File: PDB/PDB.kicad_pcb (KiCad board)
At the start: 2 copper layers, 0 parts

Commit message: more footprint
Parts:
- added C1: 4.7uF, Capacitor_SMD:C_0603_1608Metric, F.Cu at (390.8, 77.3)
- added C10: 470nF, Capacitor_SMD:C_0603_1608Metric, F.Cu at (394.8, 84.8)
- added C11: 470nF, Capacitor_SMD:C_0603_1608Metric, F.Cu at (394.8, 87.3)
- added C12: 1.5uF, Capacitor_SMD:C_0603_1608Metric, F.Cu at (394.8, 89.8)
- added C13: 1.5uF, Capacitor_SMD:C_0603_1608Metric, F.Cu at (398.9, 77.3)
- added C14: 100nf, Capacitor_SMD:C_0603_1608Metric, F.Cu at (398.9, 79.8)
- added C15: 100nf, Capacitor_SMD:C_0603_1608Metric, F.Cu at (424.1, 104.4)
- added C16: 100nf, Capacitor_SMD:C_0603_1608Metric, F.Cu at (438.6, 132.3)
- added C17: 100nf, Capacitor_SMD:C_0603_1608Metric, F.Cu at (424.1, 132.3)
- added C18: 100nf, Capacitor_SMD:C_0603_1608Metric, F.Cu at (377.8, 104.4)
- added C19: 100nf, Capacitor_SMD:C_0603_1608Metric, F.Cu at (377.8, 106.9)
- added C2: 100nF, Capacitor_SMD:C_0603_1608Metric, F.Cu at (390.8, 79.8)
- added C20: 4.7uF, Capacitor_SMD:C_0603_1608Metric_Pad1.08x0.95mm_HandSolder, F.Cu at (320.8, 104.4)
- added C21: 470nF, Capacitor_SMD:C_0603_1608Metric_Pad1.08x0.95mm_HandSolder, F.Cu at (320.8, 106.9)
- added C22: 2.2uF, Capacitor_SMD:C_0603_1608Metric_Pad1.08x0.95mm_HandSolder, F.Cu at (320.8, 109.4)
- added C23: 470nF, Capacitor_SMD:C_0603_1608Metric_Pad1.08x0.95mm_HandSolder, F.Cu at (320.8, 111.9)
- added C24: 68uF, Capacitor_SMD:C_0603_1608Metric_Pad1.08x0.95mm_HandSolder, F.Cu at (320.8, 114.4)
- added C25: 68uF, Capacitor_SMD:C_0603_1608Metric_Pad1.08x0.95mm_HandSolder, F.Cu at (320.8, 116.9)
- added C26: 68uF, Capacitor_SMD:C_0603_1608Metric_Pad1.08x0.95mm_HandSolder, F.Cu at (320.8, 119.4)
- added C27: 470nF, Capacitor_SMD:C_0603_1608Metric_Pad1.08x0.95mm_HandSolder, F.Cu at (320.8, 122.0)
- added C28: 10uF, Capacitor_SMD:C_0603_1608Metric_Pad1.08x0.95mm_HandSolder, F.Cu at (320.8, 124.5)
- added C29: 10uF, Capacitor_SMD:C_0603_1608Metric_Pad1.08x0.95mm_HandSolder, F.Cu at (325.2, 104.4)
- added C3: 100nF, Capacitor_SMD:C_0603_1608Metric, F.Cu at (390.8, 82.3)
- added C30: 220nF, Capacitor_SMD:C_0603_1608Metric_Pad1.08x0.95mm_HandSolder, F.Cu at (325.2, 106.9)
- added C31: 100nF, Capacitor_SMD:C_0603_1608Metric_Pad1.08x0.95mm_HandSolder, F.Cu at (325.2, 109.4)
- added C32: 100pF, Capacitor_SMD:C_0603_1608Metric_Pad1.08x0.95mm_HandSolder, F.Cu at (325.2, 111.9)
- added C33: 220uF, Capacitor_SMD:C_0603_1608Metric_Pad1.08x0.95mm_HandSolder, F.Cu at (325.2, 114.4)
- added C34: 10uF, Capacitor_SMD:C_0603_1608Metric_Pad1.08x0.95mm_HandSolder, F.Cu at (325.2, 116.9)
- added C35: 1uF, Capacitor_SMD:C_0603_1608Metric_Pad1.08x0.95mm_HandSolder, F.Cu at (325.2, 119.4)
- added C36: 1uF, Capacitor_SMD:C_0603_1608Metric_Pad1.08x0.95mm_HandSolder, F.Cu at (325.2, 122.0)
- added C37: 1uF, Capacitor_SMD:C_0603_1608Metric_Pad1.08x0.95mm_HandSolder, F.Cu at (325.2, 124.5)
- added C38: 100nf, Capacitor_SMD:C_0603_1608Metric, F.Cu at (332.8, 127.0)
- added C39: 10uF, Capacitor_SMD:C_0603_1608Metric_Pad1.08x0.95mm_HandSolder, F.Cu at (329.5, 104.4)
- added C4: 100nF, Capacitor_SMD:C_0603_1608Metric, F.Cu at (390.8, 84.8)
- added C40: 100nf, Capacitor_SMD:C_0603_1608Metric, F.Cu at (391.9, 104.4)
- added C5: 100nF, Capacitor_SMD:C_0603_1608Metric, F.Cu at (390.8, 87.3)
- added C6: 100nF, Capacitor_SMD:C_0603_1608Metric, F.Cu at (390.8, 89.8)
- added C7: 100nF, Capacitor_SMD:C_0603_1608Metric, F.Cu at (394.8, 77.3)
- added C8: 2.2uF, Capacitor_SMD:C_0603_1608Metric, F.Cu at (394.8, 79.8)
- added C9: 2.2uF, Capacitor_SMD:C_0603_1608Metric, F.Cu at (394.8, 82.3)
- added Cboot1: 08053C104KAT2A, Capacitor_SMD:C_0603_1608Metric, F.Cu at (424.1, 106.9)
- added Cboot2: 470nF, Capacitor_SMD:C_0603_1608Metric, F.Cu at (438.6, 134.8)
- added Cboot3: 100nF, Capacitor_SMD:C_0603_1608Metric, F.Cu at (377.8, 109.4)
- added Cboot4: 08053C104JAZ2A, Capacitor_SMD:C_0603_1608Metric, F.Cu at (391.9, 106.9)
- added Ccomp1: C0402C150J4GACTU, Capacitor_SMD:C_0603_1608Metric, F.Cu at (424.1, 109.4)
- added Ccomp2: 04025A471JAT2A, Capacitor_SMD:C_0603_1608Metric, F.Cu at (424.1, 111.9)
- added Ccomp3: 47nF, Capacitor_SMD:C_0603_1608Metric, F.Cu at (377.8, 111.9)
- added Ccomp4: 820pF, Capacitor_SMD:C_0603_1608Metric, F.Cu at (377.8, 114.4)
- added Ccomp5: CGA4J2C0G1H333J125AA, Capacitor_SMD:C_0603_1608Metric, F.Cu at (391.9, 109.4)
- added Ccomp6: GRM1555C1H391JA01J, Capacitor_SMD:C_0603_1608Metric, F.Cu at (391.9, 111.9)
- added Cin1: C3225X7R2A225K230AB, Capacitor_SMD:C_0603_1608Metric, F.Cu at (424.1, 114.4)
- added Cin2: 4.7uF, Capacitor_SMD:C_0603_1608Metric, F.Cu at (438.6, 137.3)
- added Cin3: 4.7 uF, Capacitor_SMD:C_0603_1608Metric, F.Cu at (424.1, 134.8)
- added Cin4: 15uF, Capacitor_SMD:C_0603_1608Metric, F.Cu at (377.8, 116.9)
- added Cin5: 100SXV15M, Capacitor_SMD:C_0603_1608Metric, F.Cu at (391.9, 114.4)
- added Cin_1: 100SXV15M, Capacitor_SMD:C_0603_1608Metric, F.Cu at (391.9, 116.9)
- added Cin_2: 100SXV15M, Capacitor_SMD:C_0603_1608Metric, F.Cu at (391.9, 119.4)
- added Cinx1: C2012X7R2A104K125AA, Capacitor_SMD:C_0603_1608Metric, F.Cu at (428.1, 104.4)
- added Cinx2: 470nF, Capacitor_SMD:C_0603_1608Metric, F.Cu at (438.6, 139.8)
- added Cinx3: 100nF, Capacitor_SMD:C_0603_1608Metric, F.Cu at (377.8, 119.4)
- added Cinx4: C2012X7R2A104K125AA, Capacitor_SMD:C_0603_1608Metric, F.Cu at (395.9, 104.4)
- added Cout1: GRM32ER61C476KE15L, Capacitor_SMD:C_0603_1608Metric, F.Cu at (428.1, 106.9)
- added Cout2: 220uF, Capacitor_SMD:C_0603_1608Metric, F.Cu at (442.6, 132.3)
- added Cout3: 22uF, Capacitor_SMD:C_0603_1608Metric, F.Cu at (424.1, 137.3)
- added Cout4: 22uF, Capacitor_SMD:C_0603_1608Metric, F.Cu at (377.8, 122.0)
- added Cout5: EEHZC1E331P, Capacitor_SMD:C_0603_1608Metric, F.Cu at (395.9, 106.9)
- added Cout_1: GRM32ER61C476KE15L, Capacitor_SMD:C_0603_1608Metric, F.Cu at (428.1, 109.4)
- added Cout_2: EEHZC1E331P, Capacitor_SMD:C_0603_1608Metric, F.Cu at (395.9, 109.4)
- added Coutx1: 470nF, Capacitor_SMD:C_0603_1608Metric, F.Cu at (442.6, 134.8)
- added Coutx2: 470nF, Capacitor_SMD:C_0603_1608Metric, F.Cu at (381.8, 104.4)
- added Coutx3: 470nF, Capacitor_SMD:C_0603_1608Metric, F.Cu at (381.8, 106.9)
- added Coutx4: C1005X6S1C474K050BC, Capacitor_SMD:C_0603_1608Metric, F.Cu at (395.9, 111.9)
- added Coutx5: C1005X6S1C474K050BC, Capacitor_SMD:C_0603_1608Metric, F.Cu at (395.9, 114.4)
- added Cramp1: GRM1555C1H241GA01D, Capacitor_SMD:C_0603_1608Metric, F.Cu at (428.1, 111.9)
- added Cramp2: 680pF, Capacitor_SMD:C_0603_1608Metric, F.Cu at (381.8, 109.4)
- added Cramp3: CL05C821JB5NNNC, Capacitor_SMD:C_0603_1608Metric, F.Cu at (395.9, 116.9)
- added Css1: CGA4J2C0G1H333J125AA, Capacitor_SMD:C_0603_1608Metric, F.Cu at (428.1, 114.4)
- added Css2: 22nF, Capacitor_SMD:C_0603_1608Metric, F.Cu at (381.8, 111.9)
- added Css3: C2012C0G1H223K125AA, Capacitor_SMD:C_0603_1608Metric, F.Cu at (395.9, 119.4)
- added Cvcc1: C1005X5R1E105K050BC, Capacitor_SMD:C_0603_1608Metric, F.Cu at (432.1, 104.4)
- added Cvcc2: 2.2uF, Capacitor_SMD:C_0603_1608Metric, F.Cu at (442.6, 137.3)
- added Cvcc3: 1uF, Capacitor_SMD:C_0603_1608Metric, F.Cu at (381.8, 114.4)
- added Cvcc4: C1005X5R1E105K050BC, Capacitor_SMD:C_0603_1608Metric, F.Cu at (399.9, 104.4)
- added D1: LED, LED_SMD:LED_0805_2012Metric, F.Cu at (407.1, 77.5)
- added D10: DDZ9699T 12V, Diode_SMD:D_SOD-523, F.Cu at (451.6, 77.3)
- added D11: DDZ9699T 12V, Diode_SMD:D_SOD-523, F.Cu at (451.6, 79.7)
- added D12: BAS516,115, Diode_SMD:D_SOD-523, F.Cu at (441.5, 121.0)
- added D13: LED, LED_SMD:LED_0805_2012Metric, F.Cu at (440.4, 125.5)
- added D14: LED, LED_SMD:LED_0805_2012Metric, F.Cu at (450.9, 132.6)
- added D15: LED, LED_SMD:LED_0805_2012Metric, F.Cu at (428.4, 143.9)
- added D16: 850mV, Diode_SMD:D_SOD-523, F.Cu at (385.0, 124.4)
- added D17: 950mV, Diode_SMD:D_SOD-523, F.Cu at (385.0, 126.9)
- added D18: LED, LED_SMD:LED_0805_2012Metric, F.Cu at (368.9, 128.3)
- added D19: STPS5L25B, Package_TO_SOT_SMD:TO-252-2, F.Cu at (325.6, 129.9)
- added D2: LED, LED_SMD:LED_0805_2012Metric, F.Cu at (407.1, 80.6)
- added D20: LED, LED_SMD:LED_0805_2012Metric, F.Cu at (350.4, 129.6)
- added D21: SBRD10200TR, Package_TO_SOT_SMD:TO-252-2_TabPin1, F.Cu at (413.8, 107.6)
- added D22: SB20150TR, Diode_THT:D_5W_P10.16mm_Horizontal, F.Cu at (392.0, 123.3)
- added D23: LED, LED_SMD:LED_0805_2012Metric, F.Cu at (416.6, 129.8)
- added D3: LED, LED_SMD:LED_0805_2012Metric, F.Cu at (407.1, 83.6)
- added D4: LED, LED_SMD:LED_0805_2012Metric, F.Cu at (407.1, 86.7)
- added D5: LED, LED_SMD:LED_0805_2012Metric, F.Cu at (407.1, 89.7)
- added D6: SMAJ64A, Diode_SMD:D_SMA, F.Cu at (362.4, 78.3)
- added D7: SMAJ64A, Diode_SMD:D_SMA, F.Cu at (362.4, 82.9)
- added D8: SMAJ64A, Diode_SMD:D_SMA, F.Cu at (362.4, 87.4)
- added D9: SMAJ64A, Diode_SMD:D_SMA, F.Cu at (362.4, 92.0)
- added F1: TR/3216FF15-R, Fuse:Fuse_1206_3216Metric, F.Cu at (441.0, 111.5)
- added F2: TR/3216FF15-R, Fuse:Fuse_1206_3216Metric, F.Cu at (446.7, 146.2)
- added F3: TR/3216FF15-R, Fuse:Fuse_1206_3216Metric, F.Cu at (428.9, 140.7)
- added F4: TR/3216FF15-R, Fuse:Fuse_1206_3216Metric, F.Cu at (363.8, 128.4)
- added F5: TR/3216FF15-R, Fuse:Fuse_1206_3216Metric, F.Cu at (345.2, 130.7)
- added F6: TR/3216FF15-R, Fuse:Fuse_1206_3216Metric, F.Cu at (417.1, 126.6)
- added J1: Micro_SD_Card, Connector_Card:microSD_HC_Hirose_DM3AT-SF-PEJM5, F.Cu at (331.4, 85.4)
- added J13: RJ45_Abracon_ARJP11A-MASA-B-A-EMU2, Connector_RJ:RJ45_Abracon_ARJP11A-MA_Horizontal, F.Cu at (359.8, 106.0)
- added J14: USB_C_Receptacle, Connector_USB:USB_C_Receptacle_CNCTech_C-ARA1-AK51X, F.Cu at (341.9, 108.5)
- added J15: XT90PW-M, Connector_AMASS:AMASS_XT90PW-M_1x02_P10.90mm_Horizontal, F.Cu at (324.6, 71.4)
- added J16: XT90PW-M, Connector_AMASS:AMASS_XT90PW-M_1x02_P10.90mm_Horizontal, F.Cu at (347.5, 71.4)
- added J17: XT90PW-M, Connector_AMASS:AMASS_XT90PW-M_1x02_P10.90mm_Horizontal, F.Cu at (370.3, 71.4)
- added J18: XT90PW-M, Connector_AMASS:AMASS_XT90PW-M_1x02_P10.90mm_Horizontal, F.Cu at (393.2, 71.4)
- added J19: XT90PW-M, Connector_AMASS:AMASS_XT90PW-M_1x02_P10.90mm_Horizontal, F.Cu at (416.0, 71.4)
- added J2: XT30PW-M, Connector_AMASS:AMASS_XT30U-F_1x02_P5.0mm_Vertical, F.Cu at (412.9, 79.7)
- added J20: XT90PW-M, Connector_AMASS:AMASS_XT90PW-M_1x02_P10.90mm_Horizontal, F.Cu at (438.9, 71.4)
- added J3: XT30PW-M, Connector_AMASS:AMASS_XT30U-F_1x02_P5.0mm_Vertical, F.Cu at (412.9, 86.9)
- added J4: XT60PW-M, Connector_AMASS:AMASS_XT60-F_1x02_P7.20mm_Vertical, F.Cu at (376.5, 81.2)
- added J6: UART OUT, Connector_PinHeader_2.54mm:PinHeader_1x04_P2.54mm_Vertical, F.Cu at (423.9, 84.3)
- added J9: swd, Connector_PinHeader_2.54mm:PinHeader_1x02_P2.54mm_Vertical, F.Cu at (442.3, 78.3)
- added L1: XAL7070-222MEB, Inductor_SMD:L_1206_3216Metric, F.Cu at (441.0, 108.2)
- added L2: 8.2uH, Inductor_SMD:L_1206_3216Metric, F.Cu at (446.8, 142.8)
- added L3: 1uH, Inductor_SMD:L_1206_3216Metric, F.Cu at (429.0, 137.4)
- added L4: 33uH, Inductor_SMD:L_1206_3216Metric, F.Cu at (358.2, 128.5)
- added L5: 10uH, Inductor_SMD:L_1206_3216Metric, F.Cu at (345.3, 123.9)
- added L6: 10uH, Inductor_SMD:L_1206_3216Metric, F.Cu at (345.3, 127.3)
- added L7: 15uH, Inductor_SMD:L_1206_3216Metric, F.Cu at (400.0, 127.7)
- added M1: GENERIC_MOSFET_N, Package_SON:Infineon_PG-TDSON-8_6.15x5.15mm, F.Cu at (426.7, 119.0)
- added M2: GENERIC_MOSFET_N, Package_SON:Infineon_PG-TDSON-8_6.15x5.15mm, F.Cu at (426.7, 125.7)
- added M3: CSD19502Q5B, Dependencies:CSD19502Q5B, F.Cu at (410.5, 115.1)
- added M4: CSD17578Q3A, Dependencies:CSD19502Q5B, F.Cu at (410.5, 121.7)
- added Q1: IPT012N08N5, Package_TO_SOT_SMD:SOT-23, F.Cu at (368.8, 78.3)
- added Q2: IPT012N08N5, Package_TO_SOT_SMD:SOT-23, F.Cu at (368.8, 82.7)
- added Q3: BSC093N15NS5, Package_TO_SOT_SMD:SOT-23, F.Cu at (368.8, 87.2)
- added Q4: BSC093N15NS5, Package_TO_SOT_SMD:SOT-23, F.Cu at (368.8, 91.6)
- added Q5: CSD19502Q5B, Dependencies:CSD19502Q5B, F.Cu at (352.1, 145.0)
- added Q6: CSD19502Q5B, Dependencies:CSD19502Q5B, F.Cu at (341.9, 145.0)
- added Q7: STL6P3LLH6, Dependencies:CSD19502Q5B, F.Cu at (362.3, 147.6)
- added Q8: STL6P3LLH6, Dependencies:CSD19502Q5B, F.Cu at (362.3, 154.1)
- added R1: 47k, Resistor_SMD:R_0603_1608Metric, F.Cu at (398.9, 82.3)
- added R10: 270, Resistor_SMD:R_0603_1608Metric, F.Cu at (402.9, 89.8)
- added R11: 10k, Resistor_SMD:R_0603_1608Metric_Pad0.98x0.95mm_HandSolder, F.Cu at (320.8, 77.3)
- added R12: 10k, Resistor_SMD:R_0603_1608Metric_Pad0.98x0.95mm_HandSolder, F.Cu at (320.8, 79.8)
- added R13: 10k, Resistor_SMD:R_0603_1608Metric_Pad0.98x0.95mm_HandSolder, F.Cu at (320.8, 82.3)
- added R14: 10k, Resistor_SMD:R_0603_1608Metric_Pad0.98x0.95mm_HandSolder, F.Cu at (320.8, 84.8)
- added R15: 10k, Resistor_SMD:R_0603_1608Metric_Pad0.98x0.95mm_HandSolder, F.Cu at (320.8, 87.3)
- added R16: 10k, Resistor_SMD:R_0603_1608Metric_Pad0.98x0.95mm_HandSolder, F.Cu at (320.8, 89.8)
- added R17: 1k, Resistor_SMD:R_0603_1608Metric_Pad0.98x0.95mm_HandSolder, F.Cu at (320.8, 92.3)
- added R18: 1k, Resistor_SMD:R_0603_1608Metric_Pad0.98x0.95mm_HandSolder, F.Cu at (320.8, 94.9)
- added R19: 100k, Resistor_SMD:R_0603_1608Metric_Pad0.98x0.95mm_HandSolder, F.Cu at (320.8, 97.4)
- added R2: 47k, Resistor_SMD:R_0603_1608Metric, F.Cu at (398.9, 84.8)
- added R20: 100k, Resistor_SMD:R_0603_1608Metric_Pad0.98x0.95mm_HandSolder, F.Cu at (320.8, 99.9)
- added R21: R_Shunt, Resistor_SMD:R_0603_1608Metric, F.Cu at (432.1, 106.9)
- added R22: 270, Resistor_SMD:R_1206_3216Metric_Pad1.30x1.75mm_HandSolder, F.Cu at (441.1, 104.8)
- added R23: 270, Resistor_SMD:R_0603_1608Metric, F.Cu at (442.6, 139.8)
- added R24: R_Shunt, Resistor_SMD:R_0603_1608Metric, F.Cu at (446.6, 132.3)
- added R25: 270, Resistor_SMD:R_0603_1608Metric, F.Cu at (424.1, 139.8)
- added R26: R_Shunt, Resistor_SMD:R_0603_1608Metric, F.Cu at (424.1, 142.4)
- added R27: R_Shunt, Resistor_SMD:R_0603_1608Metric, F.Cu at (381.8, 116.9)
- added R28: 270, Resistor_SMD:R_1206_3216Metric_Pad1.30x1.75mm_HandSolder, F.Cu at (378.8, 129.4)
- added R29: 100k, Resistor_SMD:R_0603_1608Metric_Pad0.98x0.95mm_HandSolder, F.Cu at (329.5, 106.9)
- added R3: 47k, Resistor_SMD:R_0603_1608Metric, F.Cu at (398.9, 87.3)
- added R30: 100k, Resistor_SMD:R_0603_1608Metric_Pad0.98x0.95mm_HandSolder, F.Cu at (329.5, 109.4)
- added R31: 11.1k, Resistor_SMD:R_0603_1608Metric_Pad0.98x0.95mm_HandSolder, F.Cu at (329.5, 111.9)
- added R32: 200k, Resistor_SMD:R_0603_1608Metric_Pad0.98x0.95mm_HandSolder, F.Cu at (329.5, 114.4)
- added R33: 13k, Resistor_SMD:R_0603_1608Metric_Pad0.98x0.95mm_HandSolder, F.Cu at (329.5, 116.9)
- added R34: 4.7k, Resistor_SMD:R_0603_1608Metric_Pad0.98x0.95mm_HandSolder, F.Cu at (329.5, 119.4)
- added R35: 4.87k, Resistor_SMD:R_0603_1608Metric_Pad0.98x0.95mm_HandSolder, F.Cu at (329.5, 122.0)
- added R36: 8.66k, Resistor_SMD:R_0603_1608Metric_Pad0.98x0.95mm_HandSolder, F.Cu at (329.5, 124.5)
- added R37: 33k, Resistor_SMD:R_0603_1608Metric_Pad0.98x0.95mm_HandSolder, F.Cu at (333.9, 104.4)
- added R38: 100k, Resistor_SMD:R_0603_1608Metric_Pad0.98x0.95mm_HandSolder, F.Cu at (333.9, 106.9)
- added R39: 82, Resistor_SMD:R_0603_1608Metric_Pad0.98x0.95mm_HandSolder, F.Cu at (333.9, 109.4)
- added R4: 47k, Resistor_SMD:R_0603_1608Metric, F.Cu at (398.9, 89.8)
- added R40: 10k, Resistor_SMD:R_0603_1608Metric_Pad0.98x0.95mm_HandSolder, F.Cu at (333.9, 111.9)
- added R41: 10k, Resistor_SMD:R_0603_1608Metric_Pad0.98x0.95mm_HandSolder, F.Cu at (333.9, 114.4)
- added R42: 2.2k, Resistor_SMD:R_0603_1608Metric_Pad0.98x0.95mm_HandSolder, F.Cu at (333.9, 116.9)
- added R43: R_Shunt, Resistor_SMD:R_0603_1608Metric, F.Cu at (332.8, 129.5)
- added R44: 270, Resistor_SMD:R_1206_3216Metric_Pad1.30x1.75mm_HandSolder, F.Cu at (339.0, 130.5)
- added R45: R_Shunt, Resistor_SMD:R_0603_1608Metric, F.Cu at (399.9, 106.9)
- added R46: 270, Capacitor_SMD:C_0603_1608Metric, F.Cu at (399.9, 109.4)
- added R5: 47k, Resistor_SMD:R_0603_1608Metric, F.Cu at (402.9, 77.3)
- added R6: 270, Resistor_SMD:R_0603_1608Metric, F.Cu at (402.9, 79.8)
- added R7: 270, Resistor_SMD:R_0603_1608Metric, F.Cu at (402.9, 82.3)
- added R8: 270, Resistor_SMD:R_0603_1608Metric, F.Cu at (402.9, 84.8)
- added R9: 270, Resistor_SMD:R_0603_1608Metric, F.Cu at (402.9, 87.3)
- added Rcomp1: CRCW040246K4FKED, Resistor_SMD:R_0603_1608Metric, F.Cu at (432.1, 109.4)
- added Rcomp2: 12.1kOhm, Resistor_SMD:R_0603_1608Metric, F.Cu at (381.8, 119.4)
- added Rcomp3: RC0201FR-0723K7L, Resistor_SMD:R_0603_1608Metric, F.Cu at (399.9, 111.9)
- added Renable1: CRCW04021M00FKED, Resistor_SMD:R_0603_1608Metric, F.Cu at (432.1, 111.9)
- added Renable2: 1MOhm, Resistor_SMD:R_0603_1608Metric, F.Cu at (381.8, 122.0)
- added Renable3: CRCW04021M00FKED, Resistor_SMD:R_0603_1608Metric, F.Cu at (399.9, 114.4)
- added Rfbb1: RT0805BRD0710K4L, Resistor_SMD:R_0603_1608Metric, F.Cu at (432.1, 114.4)
- added Rfbb2: 24.9kOhm, Resistor_SMD:R_0603_1608Metric, F.Cu at (446.6, 134.8)
- added Rfbb3: 100kOhm, Resistor_SMD:R_0603_1608Metric, F.Cu at (424.1, 144.9)
- added Rfbb4: 1kOhm, Resistor_SMD:R_0603_1608Metric, F.Cu at (385.9, 104.4)
- added Rfbb5: CRCW04021K00FKED, Resistor_SMD:R_0603_1608Metric, F.Cu at (399.9, 116.9)
- added Rfbt1: ERJ-6ENF3242V, Resistor_SMD:R_0603_1608Metric, F.Cu at (436.1, 104.4)
- added Rfbt2: 100kOhm, Resistor_SMD:R_0603_1608Metric, F.Cu at (446.6, 137.3)
- added Rfbt3: 453kOhm, Resistor_SMD:R_0603_1608Metric, F.Cu at (424.1, 147.4)
- added Rfbt4: 18.7kOhm, Resistor_SMD:R_0603_1608Metric, F.Cu at (385.9, 106.9)
- added Rfbt5: CRCW04028K66FKED, Resistor_SMD:R_0603_1608Metric, F.Cu at (399.9, 119.4)
- added Rpgood1: 100kOhm, Resistor_SMD:R_0603_1608Metric, F.Cu at (446.6, 139.8)
- added Rramp1: 105kOhm, Resistor_SMD:R_0603_1608Metric, F.Cu at (385.9, 109.4)
- added Rsense1: PRL1632-R005-F-T1, Resistor_SMD:R_0603_1608Metric, F.Cu at (436.1, 106.9)
- added Rsense2: 25mOhm, Resistor_SMD:R_0603_1608Metric, F.Cu at (385.9, 111.9)
- added Rsense3: CRA2512-FZ-R010ELF, Resistor_SMD:R_0603_1608Metric, F.Cu at (403.9, 104.4)
- added Rt1: CRCW04026K65FKED, Resistor_SMD:R_0603_1608Metric, F.Cu at (436.1, 109.4)
- added Rt2: 18.7kOhm, Resistor_SMD:R_0603_1608Metric, F.Cu at (385.9, 114.4)
- added Rt3: CRCW040246K4FKED, Resistor_SMD:R_0603_1608Metric, F.Cu at (403.9, 106.9)
- added Ruv1: CRCW080564K9FKEA, Resistor_SMD:R_0603_1608Metric, F.Cu at (436.1, 111.9)
- added Ruv2: ERJ-6ENF9091V, Resistor_SMD:R_0603_1608Metric, F.Cu at (436.1, 114.4)
- added Ruv3: 64.9kOhm, Resistor_SMD:R_0603_1608Metric, F.Cu at (385.9, 116.9)
- added Ruv4: 10kOhm, Resistor_SMD:R_0603_1608Metric, F.Cu at (385.9, 119.4)
- added Ruv5: CRCW040264K9FKED, Resistor_SMD:R_0603_1608Metric, F.Cu at (403.9, 109.4)
- added Ruv6: RC0201FR-0710KL, Resistor_SMD:R_0603_1608Metric, F.Cu at (403.9, 111.9)
- added S1: EG1218, Dependencies:SW_EG1218, F.Cu at (428.1, 78.8)
- added TP1: TestPoint, TestPoint:TestPoint_Pad_D2.5mm, F.Cu at (437.0, 89.3)
- added TP10: TestPoint, TestPoint:TestPoint_Pad_D2.0mm, F.Cu at (349.8, 112.7)
- added TP11: TestPoint, TestPoint:TestPoint_Pad_D2.0mm, F.Cu at (416.8, 113.9)
- added TP2: TestPoint, TestPoint:TestPoint_Pad_D2.5mm, F.Cu at (437.0, 93.8)
- added TP3: TestPoint, TestPoint:TestPoint_Pad_D2.0mm, F.Cu at (428.2, 84.0)
- added TP4: TestPoint, TestPoint:TestPoint_Pad_D2.0mm, F.Cu at (428.2, 88.1)
- added TP5: TestPoint, TestPoint:TestPoint_Pad_D2.0mm, F.Cu at (428.2, 92.1)
- added TP6: TestPoint, TestPoint:TestPoint_Pad_D2.0mm, F.Cu at (441.7, 117.7)
- added TP7: TestPoint, TestPoint:TestPoint_Pad_D2.0mm, F.Cu at (450.7, 136.1)
- added TP8: TestPoint, TestPoint:TestPoint_Pad_D2.0mm, F.Cu at (432.6, 144.4)
- added TP9: TestPoint, TestPoint:TestPoint_Pad_D2.0mm, F.Cu at (373.1, 128.8)
- added U1: STM32H742VGTx, Package_QFP:LQFP-100_14x14mm_P0.5mm, F.Cu at (349.0, 85.3)
- added U10: LM76005RNPR, Dependencies:LM76005RNPR, F.Cu at (308.2, 92.4)
- added U11: INA228, Package_SO:TSSOP-10_3x3mm_P0.5mm, F.Cu at (440.3, 143.4)
- added U12: TLV62569ADRLR, Dependencies:TLV62569ADRLR, F.Cu at (427.7, 147.0)
- added U13: INA228, Package_SO:HVSSOP-10-1EP_3x3mm_P0.5mm_EP1.83x1.89mm, F.Cu at (429.8, 133.4)
- added U14: LM5118MH, Dependencies:LM5118MH, F.Cu at (369.8, 140.5)
- added U15: INA228, Package_SO:HVSSOP-10-1EP_3x3mm_P0.5mm_EP1.83x1.89mm, F.Cu at (379.5, 125.5)
- added U16: LM76005QRNPRQ1, Dependencies:LM76005RNPR, F.Cu at (350.5, 106.9)
- added U17: ST1S14PHR, Dependencies:HSOP8_STM, F.Cu at (340.4, 118.8)
- added U18: STUSB4700YQTR, Dependencies:QFN_700QTR_STM, F.Cu at (339.2, 125.5)
- added U19: STR2P3LLH6, Dependencies:SOT_3LLH6_STM, F.Cu at (350.5, 124.9)
- added U2: MCP9804_DFN, Package_DFN_QFN:DFN-8-1EP_3x2mm_P0.5mm_EP1.7x1.4mm, F.Cu at (437.3, 77.9)
- added U20: INA228, Package_SO:HVSSOP-10-1EP_3x3mm_P0.5mm_EP1.83x1.89mm, F.Cu at (348.3, 117.8)
- added U21: LM5118MH/NOPB, Dependencies:LM5118MH, F.Cu at (410.5, 128.8)
- added U22: INA228, Package_SO:HVSSOP-10-1EP_3x3mm_P0.5mm_EP1.83x1.89mm, F.Cu at (393.5, 128.2)
- added U3: MCP9804_DFN, Package_DFN_QFN:DFN-8-1EP_3x2mm_P0.5mm_EP1.7x1.4mm, F.Cu at (437.3, 81.6)
- added U4: MCP9804_DFN, Package_DFN_QFN:DFN-8-1EP_3x2mm_P0.5mm_EP1.7x1.4mm, F.Cu at (437.3, 85.2)
- added U5: LTC4359-DCB, Package_DFN_QFN:DFN-6-1EP_3x2mm_P0.5mm_EP1.65x1.35mm, F.Cu at (447.2, 77.8)
- added U6: LTC4359-DCB, Package_DFN_QFN:DFN-6-1EP_3x2mm_P0.5mm_EP1.65x1.35mm, F.Cu at (447.2, 81.4)
- added U7: TMCS1108A4UQDRQ1, Dependencies:SOIC127P599X175-8N, F.Cu at (395.6, 142.4)
- added U8: LM5116MH/NOPB, Dependencies:MXA20A_TEX, F.Cu at (435.3, 119.8)
- added U9: INA228, Package_SO:HVSSOP-10-1EP_3x3mm_P0.5mm_EP1.83x1.89mm, F.Cu at (434.5, 126.2)
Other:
- board outline added: 114.3 x 114.3 mm

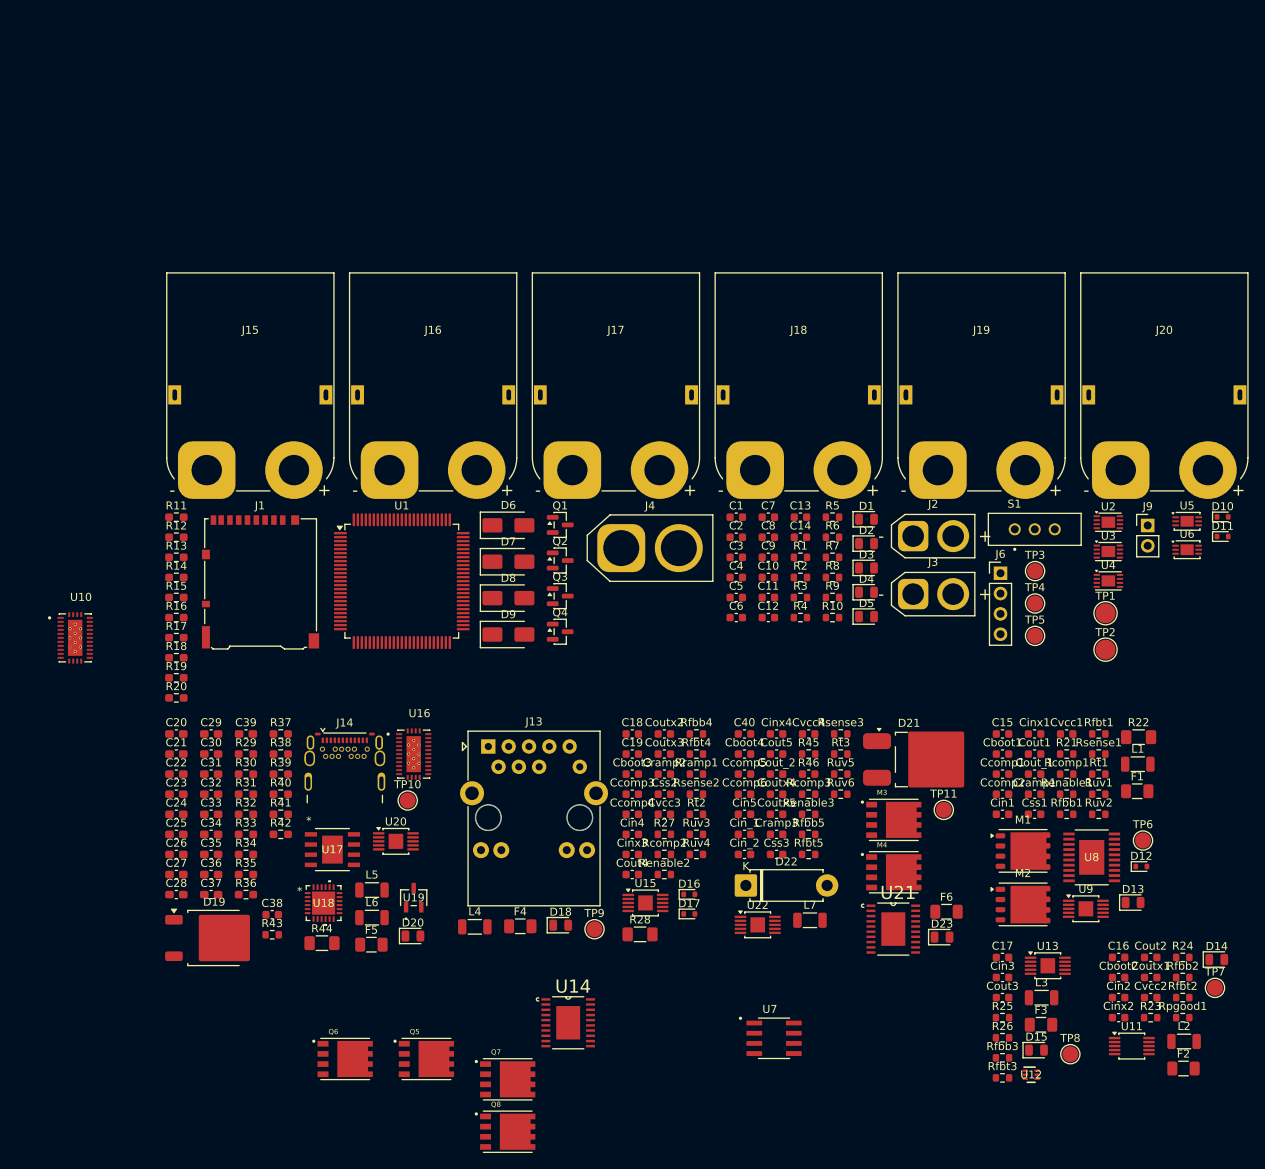
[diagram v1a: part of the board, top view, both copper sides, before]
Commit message: fixed component footprints
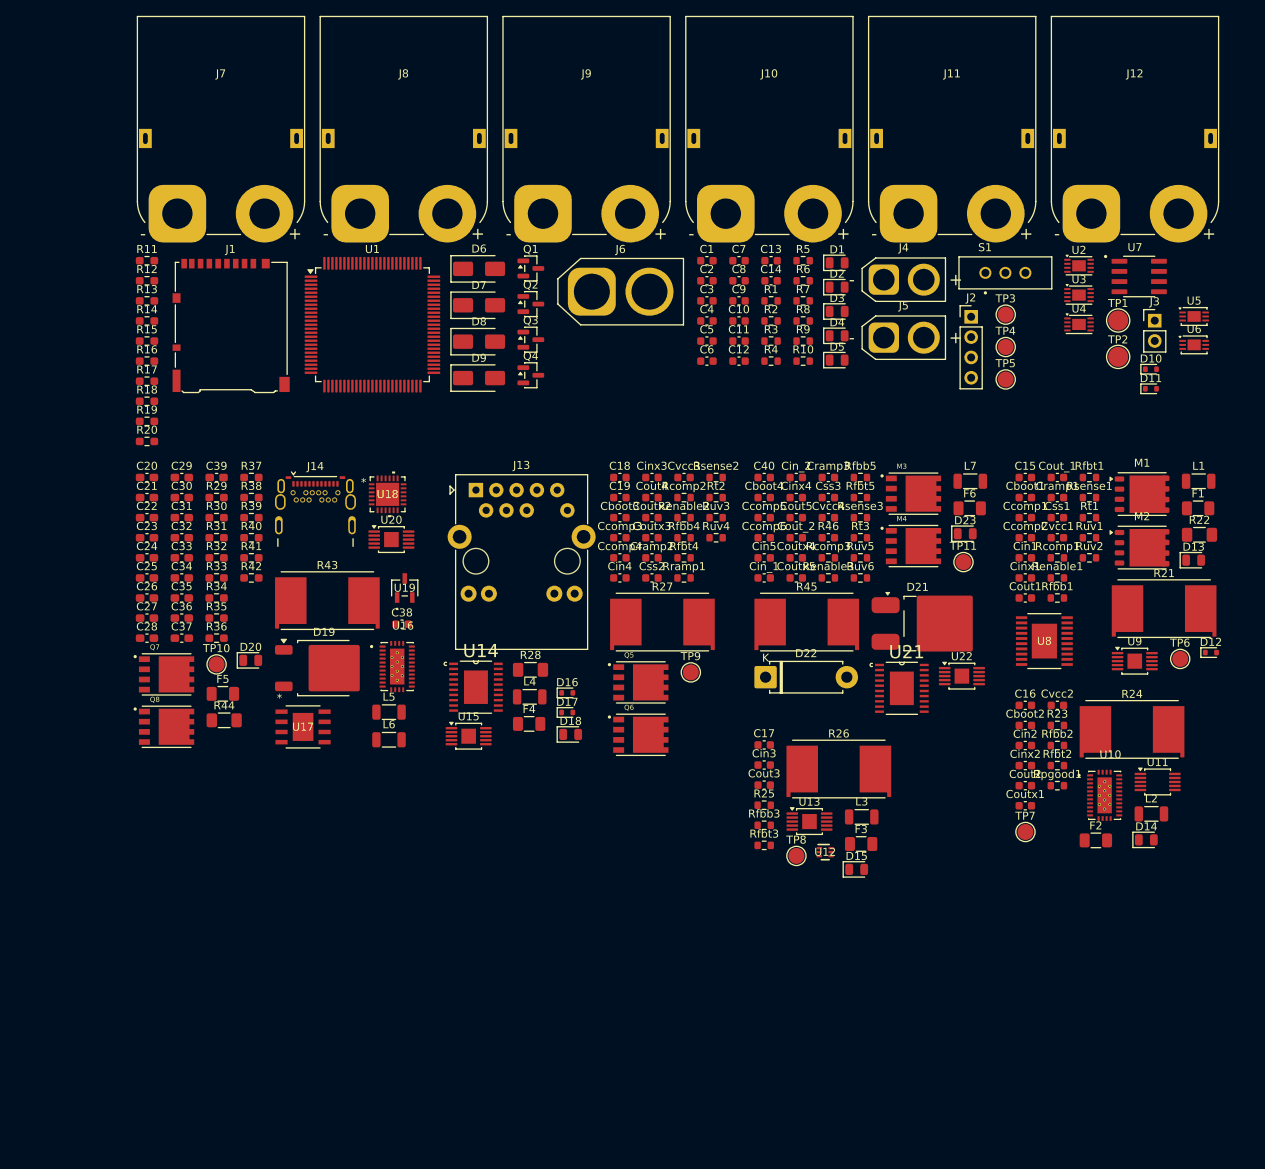
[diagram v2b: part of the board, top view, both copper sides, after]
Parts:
- removed J15, J16, J17, J18, J19, J20: XT90PW-M, Connector_AMASS:AMASS_XT90PW-M_1x02_P10.90mm_Horizontal
- added J10: XT90PW-M, Connector_AMASS:AMASS_XT90PW-M_1x02_P10.90mm_Horizontal, F.Cu at (389.5, 39.4)
- added J11: XT90PW-M, Connector_AMASS:AMASS_XT90PW-M_1x02_P10.90mm_Horizontal, F.Cu at (412.4, 39.4)
- added J12: XT90PW-M, Connector_AMASS:AMASS_XT90PW-M_1x02_P10.90mm_Horizontal, F.Cu at (435.2, 39.4)
- added J5: XT30PW-M, Connector_AMASS:AMASS_XT30U-F_1x02_P5.0mm_Vertical, F.Cu at (409.3, 54.9)
- added J7: XT90PW-M, Connector_AMASS:AMASS_XT90PW-M_1x02_P10.90mm_Horizontal, F.Cu at (321.0, 39.4)
- added J8: XT90PW-M, Connector_AMASS:AMASS_XT90PW-M_1x02_P10.90mm_Horizontal, F.Cu at (343.8, 39.4)
- J2: value XT30PW-M -> UART OUT; footprint Connector_AMASS:AMASS_XT30U-F_1x02_P5.0mm_Vertical -> Connector_PinHeader_2.54mm:PinHeader_1x04_P2.54mm_Vertical
- J3: value XT30PW-M -> swd; footprint Connector_AMASS:AMASS_XT30U-F_1x02_P5.0mm_Vertical -> Connector_PinHeader_2.54mm:PinHeader_1x02_P2.54mm_Vertical
- J4: value XT60PW-M -> XT30PW-M; footprint Connector_AMASS:AMASS_XT60-F_1x02_P7.20mm_Vertical -> Connector_AMASS:AMASS_XT30U-F_1x02_P5.0mm_Vertical
- J6: value UART OUT -> XT60PW-M; footprint Connector_PinHeader_2.54mm:PinHeader_1x04_P2.54mm_Vertical -> Connector_AMASS:AMASS_XT60-F_1x02_P7.20mm_Vertical
- J9: value swd -> XT90PW-M; footprint Connector_PinHeader_2.54mm:PinHeader_1x02_P2.54mm_Vertical -> Connector_AMASS:AMASS_XT90PW-M_1x02_P10.90mm_Horizontal
- R21, R24, R26, R27, R43, R45: footprint Resistor_SMD:R_0603_1608Metric -> Resistor_SMD:R_Shunt_Vishay_WSR2_WSR3_KelvinConnection
- moved U10 130.2 mm to (436.9, 112.1)
- moved U7 105.6 mm to (441.2, 47.2)
- moved J9 85.0 mm to (366.7, 39.4)
- moved Q7 66.2 mm to (319.6, 96.9)
- moved Q8 66.2 mm to (319.6, 103.5)
- moved J6 62.0 mm to (372.8, 49.1)
- moved L7 58.4 mm to (420.1, 72.8)
- moved Q6 54.8 mm to (378.9, 104.5)
- moved Q5 54.2 mm to (378.9, 97.9)
- moved U18 51.7 mm to (347.2, 74.4)
- moved D23 50.5 mm to (419.5, 79.4)
- moved F6 50.5 mm to (420.0, 76.2)
- moved Cin_2 47.6 mm to (398.3, 72.3)
- moved Cinx3 47.2 mm to (380.3, 72.3)
- moved Cout4 47.2 mm to (380.3, 74.8)
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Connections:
- J2 pad 1: (no net) -> /UART4_RX
- J2 pad 2: (no net) -> /UART4_TX
- J3 pad 1: (no net) -> +3.3V
- J3 pad 2: (no net) -> GND
- J6 pad 1: /UART4_RX -> (no net)
- J6 pad 2: /UART4_TX -> (no net)
- J9 pad 1: +3.3V -> (no net)
- J9 pad 2: GND -> (no net)

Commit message: Start layout
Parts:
- moved Cboot1 83.6 mm to (484.6, 135.4)
- moved Ccomp1 80.0 mm to (472.7, 143.0), turned to 180 degrees
- moved Cvcc1 79.4 mm to (484.6, 138.4)
- moved Ccomp2 78.6 mm to (470.9, 145.0)
- moved M1 77.3 mm to (490.7, 134.1)
- moved M2 76.5 mm to (490.7, 139.8)
- moved Rcomp1 76.4 mm to (474.7, 145.0)
- moved Cramp1 74.1 mm to (472.0, 136.5), turned to 180 degrees
- moved Css1 73.2 mm to (472.0, 138.0), turned to 180 degrees
- moved Cin1 69.3 mm to (472.0, 135.0), turned to 180 degrees
- moved Cinx1 66.3 mm to (472.0, 133.5), turned to 180 degrees
- moved U8 66.1 mm to (478.5, 137.0)
- moved Rt1 63.4 mm to (467.1, 132.0)
- moved Ruv2 57.0 mm to (475.0, 123.0)
- moved D12 54.8 mm to (484.6, 136.9)
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
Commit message: worked on more layout
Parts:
- moved U1 187.5 mm to (532.3, 67.4)
- moved R11 174.0 mm to (430.0, 177.7), turned to -90 degrees
- moved R14 168.4 mm to (432.6, 175.3), turned to 180 degrees
- moved C1 155.6 mm to (539.6, 76.3), turned to -90 degrees
- moved C2 154.6 mm to (541.3, 60.1)
- moved C8 152.9 mm to (541.4, 76.4), turned to 90 degrees
- moved C9 152.9 mm to (543.7, 60.8), turned to -90 degrees
- moved J1 152.8 mm to (405.9, 184.6)
- moved R10 146.7 mm to (544.7, 76.4), turned to -90 degrees
- moved R9 145.5 mm to (543.1, 76.4), turned to -90 degrees
- moved D5 141.9 mm to (543.0, 83.6), turned to 90 degrees
- moved R8 141.3 mm to (537.8, 80.0), turned to -90 degrees
- moved D4 140.5 mm to (540.9, 83.6), turned to 90 degrees
- moved R7 140.2 mm to (536.2, 80.0), turned to -90 degrees
- moved R6 139.3 mm to (534.7, 80.0), turned to -90 degrees
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
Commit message: LAYOUT
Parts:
- removed C18: 100nf, Capacitor_SMD:C_0603_1608Metric
- removed J10, J8, J9: XT90PW-M, Connector_AMASS:AMASS_XT90PW-M_1x02_P10.90mm_Horizontal
- removed J13: RJ45_Abracon_ARJP11A-MASA-B-A-EMU2, Connector_RJ:RJ45_Abracon_ARJP11A-MA_Horizontal
- removed Q6: CSD19502Q5B, Dependencies:CSD19502Q5B
- removed R12, R13, R15, R16: 10k, Resistor_SMD:R_0603_1608Metric_Pad0.98x0.95mm_HandSolder
- added C41: 100nf, Capacitor_SMD:C_0603_1608Metric, F.Cu at (371.3, 2.66)
- added C42: 0.1uF, Capacitor_SMD:C_0603_1608Metric, F.Cu at (371.3, 5.17)
- added C43: 0.1uF, Capacitor_SMD:C_0603_1608Metric, F.Cu at (371.3, 7.68)
- added F7: Fuse, Fuse:Fuse_1206_3216Metric, F.Cu at (372.1, 25.6)
- added J15: RJ45_Abracon_ARJP11A-MASA-B-A-EMU2, Connector_RJ:RJ45_Abracon_ARJP11A-MA_Horizontal, F.Cu at (111.5, 60.8)
- added R47: 47Ohm, Resistor_SMD:R_0603_1608Metric, F.Cu at (371.3, 10.2)
- added R48: 22.1Ohm, Resistor_SMD:R_0603_1608Metric, F.Cu at (371.3, 12.7)
- added R49: 1Ohm, Resistor_SMD:R_0603_1608Metric, F.Cu at (371.3, 15.2)
- added R50: 1Ohm, Resistor_SMD:R_0603_1608Metric, F.Cu at (371.3, 17.7)
- added R51: 1Ohm, Resistor_SMD:R_0603_1608Metric, F.Cu at (371.3, 20.2)
- added R52: 1Ohm, Resistor_SMD:R_0603_1608Metric, F.Cu at (371.3, 22.7)
- Ccomp3: value 47nF -> 100nF
- Ccomp4: value 820pF -> 2.2nF
- Cin4: value 15uF -> 33uF
- Cout4: value 22uF -> 15uF
- Cramp2: value 680pF -> 2.2nF
- D16: value 850mV -> 900mV
- L4: value 33uH -> 68uH
- Rcomp2: value 12.1kOhm -> 10kOhm
- Rfbt4: value 18.7kOhm -> 38.3kOhm
- Rramp1: value 105kOhm -> 36.5kOhm
- Rsense2: value 25mOhm -> 30mOhm
- moved C5 390.8 mm to (130.9, 89.1)
- moved C6 390.8 mm to (130.9, 90.8)
- moved D2 390.8 mm to (146.2, 101.8)
- moved D3 390.8 mm to (148.4, 101.8)
- moved R10 390.8 mm to (154.4, 94.6)
- moved R7 390.8 mm to (145.9, 98.3)
- moved R8 390.8 mm to (147.5, 98.3)
- moved U1 390.8 mm to (142.0, 85.6)
- moved C1 390.8 mm to (149.3, 94.6)
- moved C2 390.8 mm to (150.9, 78.3)
- moved C3 390.8 mm to (134.7, 76.6)
- moved C4 390.8 mm to (131.3, 84.5)
- moved C7 390.8 mm to (134.7, 94.5)
- moved C8 390.8 mm to (151.0, 94.6)
- moved D4 390.8 mm to (150.5, 101.8)
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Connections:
- net /24V@30W/+3.3V renamed /48V@.8A/+3.3V
- net /24V@30W/SCL renamed /48V@.8A/SCL
- net /24V@30W/SDA renamed /48V@.8A/SDA
- net 24V@1.5A renamed 48V@.8A
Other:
- board size 114.3 x 114.3 mm -> 130 x 112.6 mm

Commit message: some layout done
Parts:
- moved Rsense1 82.2 mm to (484.6, 140.4)
- moved Rfbt1 68.5 mm to (475.5, 127.5), turned to 180 degrees
- moved L1 67.1 mm to (483.9, 129.9), turned to 180 degrees
- moved Rfbb1 58.8 mm to (472.0, 129.5), turned to 180 degrees
- moved Renable1 20.0 mm to (475.5, 129.5), turned to 180 degrees
- moved Ruv1 11.3 mm to (475.5, 131.3), turned to 180 degrees
- moved Rt1 9.47 mm to (472.0, 140.1), turned to 180 degrees
- moved Ruv2 8.87 mm to (472.0, 131.3), turned to 180 degrees
- moved Ccomp2 5.51 mm to (476.4, 144.1), turned to 180 degrees
- moved Ccomp1 2.15 mm to (474.7, 142.2), turned to 0 degrees
- moved Rcomp1 1.93 mm to (473.1, 144.0), turned to 180 degrees
- moved Cinx1 0.40 mm to (472.0, 133.1)
- moved Css1 0.35 mm to (472.0, 138.3)
- moved Cboot1 0.30 mm to (484.6, 135.1)
- moved Cvcc1 0.25 mm to (484.6, 138.7)
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
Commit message: layout caps around one of the ics
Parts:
- moved Cboot1 281.5 mm to (219.9, 39.2)
- moved Ccomp1 281.5 mm to (210.0, 46.4)
- moved Ccomp2 281.5 mm to (211.7, 48.2)
- moved Cin1 281.5 mm to (207.3, 39.0)
- moved Cinx1 281.5 mm to (207.3, 37.2)
- moved Cramp1 281.5 mm to (207.3, 40.8)
- moved Css1 281.5 mm to (207.3, 42.5)
- moved Cvcc1 281.5 mm to (219.9, 42.8)
- moved D12 281.5 mm to (219.9, 41.0)
- moved L1 281.5 mm to (219.1, 34.1)
- moved M1 281.5 mm to (225.9, 38.2)
- moved M2 281.5 mm to (225.9, 44.0)
- moved Rcomp1 281.5 mm to (208.3, 48.1)
- moved Renable1 281.5 mm to (210.8, 33.6)
- moved Rfbb1 281.5 mm to (207.3, 33.6)
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
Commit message: lots of routing
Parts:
- added J10: XT90PW-M, Connector_AMASS:AMASS_XT90PW-M_1x02_P10.90mm_Horizontal, F.Cu at (260.8, 133.0)
- added J8: XT90PW-M, Connector_AMASS:AMASS_XT90PW-M_1x02_P10.90mm_Horizontal, F.Cu at (215.1, 133.0)
- added J9: XT90PW-M, Connector_AMASS:AMASS_XT90PW-M_1x02_P10.90mm_Horizontal, F.Cu at (238.0, 133.0)
- R21, R43: footprint Resistor_SMD:R_Shunt_Vishay_WSR2_WSR3_KelvinConnection -> Resistor_SMD:R_Shunt_Vishay_WSK2512_6332Metric_T2.66mm
- moved F1 287.1 mm to (457.8, 185.5)
- moved L1 286.5 mm to (459.3, 190.4)
- moved M1 285.6 mm to (466.2, 192.7)
- moved M2 285.6 mm to (466.2, 198.5)
- moved Ccomp1 285.6 mm to (450.2, 200.9)
- moved Ccomp2 285.6 mm to (451.9, 202.7)
- moved Cin1 285.6 mm to (447.5, 193.5)
- moved Cinx1 285.6 mm to (447.5, 191.8)
- moved Cout1 285.6 mm to (454.4, 183.2)
- moved Cramp1 285.6 mm to (447.5, 195.3)
- moved Css1 285.6 mm to (447.5, 197.0)
- moved Cvcc1 285.6 mm to (460.1, 197.3)
- moved D12 285.6 mm to (460.1, 195.6)
- moved Rcomp1 285.6 mm to (448.6, 202.7)
- moved Renable1 285.6 mm to (451.0, 188.2)
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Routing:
- net Net-(U18-GPIO0): track 0.00 -> 12.3 mm, vias 0 -> 2
- net Net-(U18-GPIO1): track 0.00 -> 11.6 mm, vias 0 -> 2
- net Net-(U18-GPIO2): track 0.00 -> 9.24 mm, vias 0 -> 2
- net Net-(U18-GPIO3): track 0.00 -> 7.49 mm
- net +BATT: track 0.00 -> 3.04 mm
- net Net-(U17-FB): track 0.00 -> 1.65 mm
- net GND: track 0.00 -> 1.23 mm
